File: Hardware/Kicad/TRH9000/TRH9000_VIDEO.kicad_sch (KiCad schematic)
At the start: 33 parts, among them J1 RGB, J2 S-Video, Q1 BC817, U6 CXA2075M

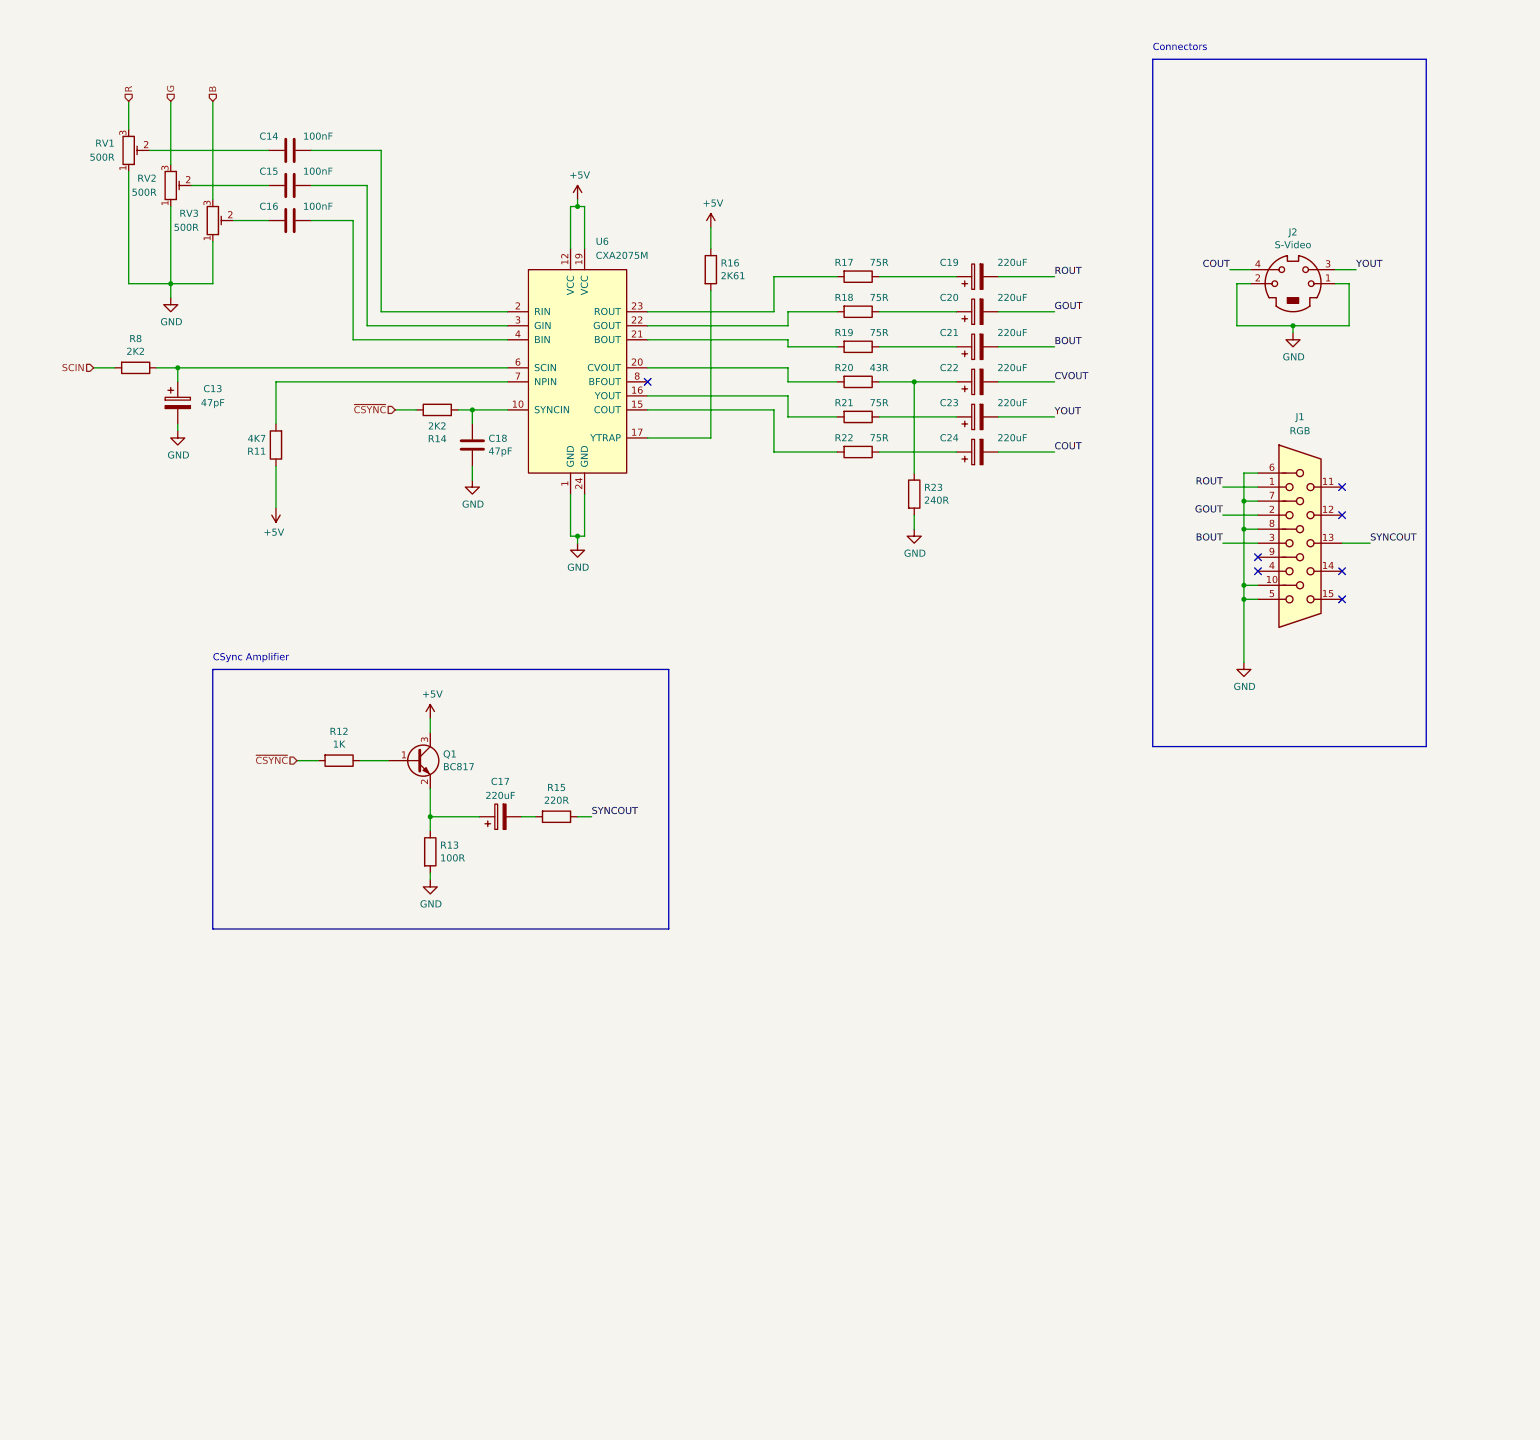
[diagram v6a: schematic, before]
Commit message: Many changes, among them, replacing the Composite out with SCART-rgb.
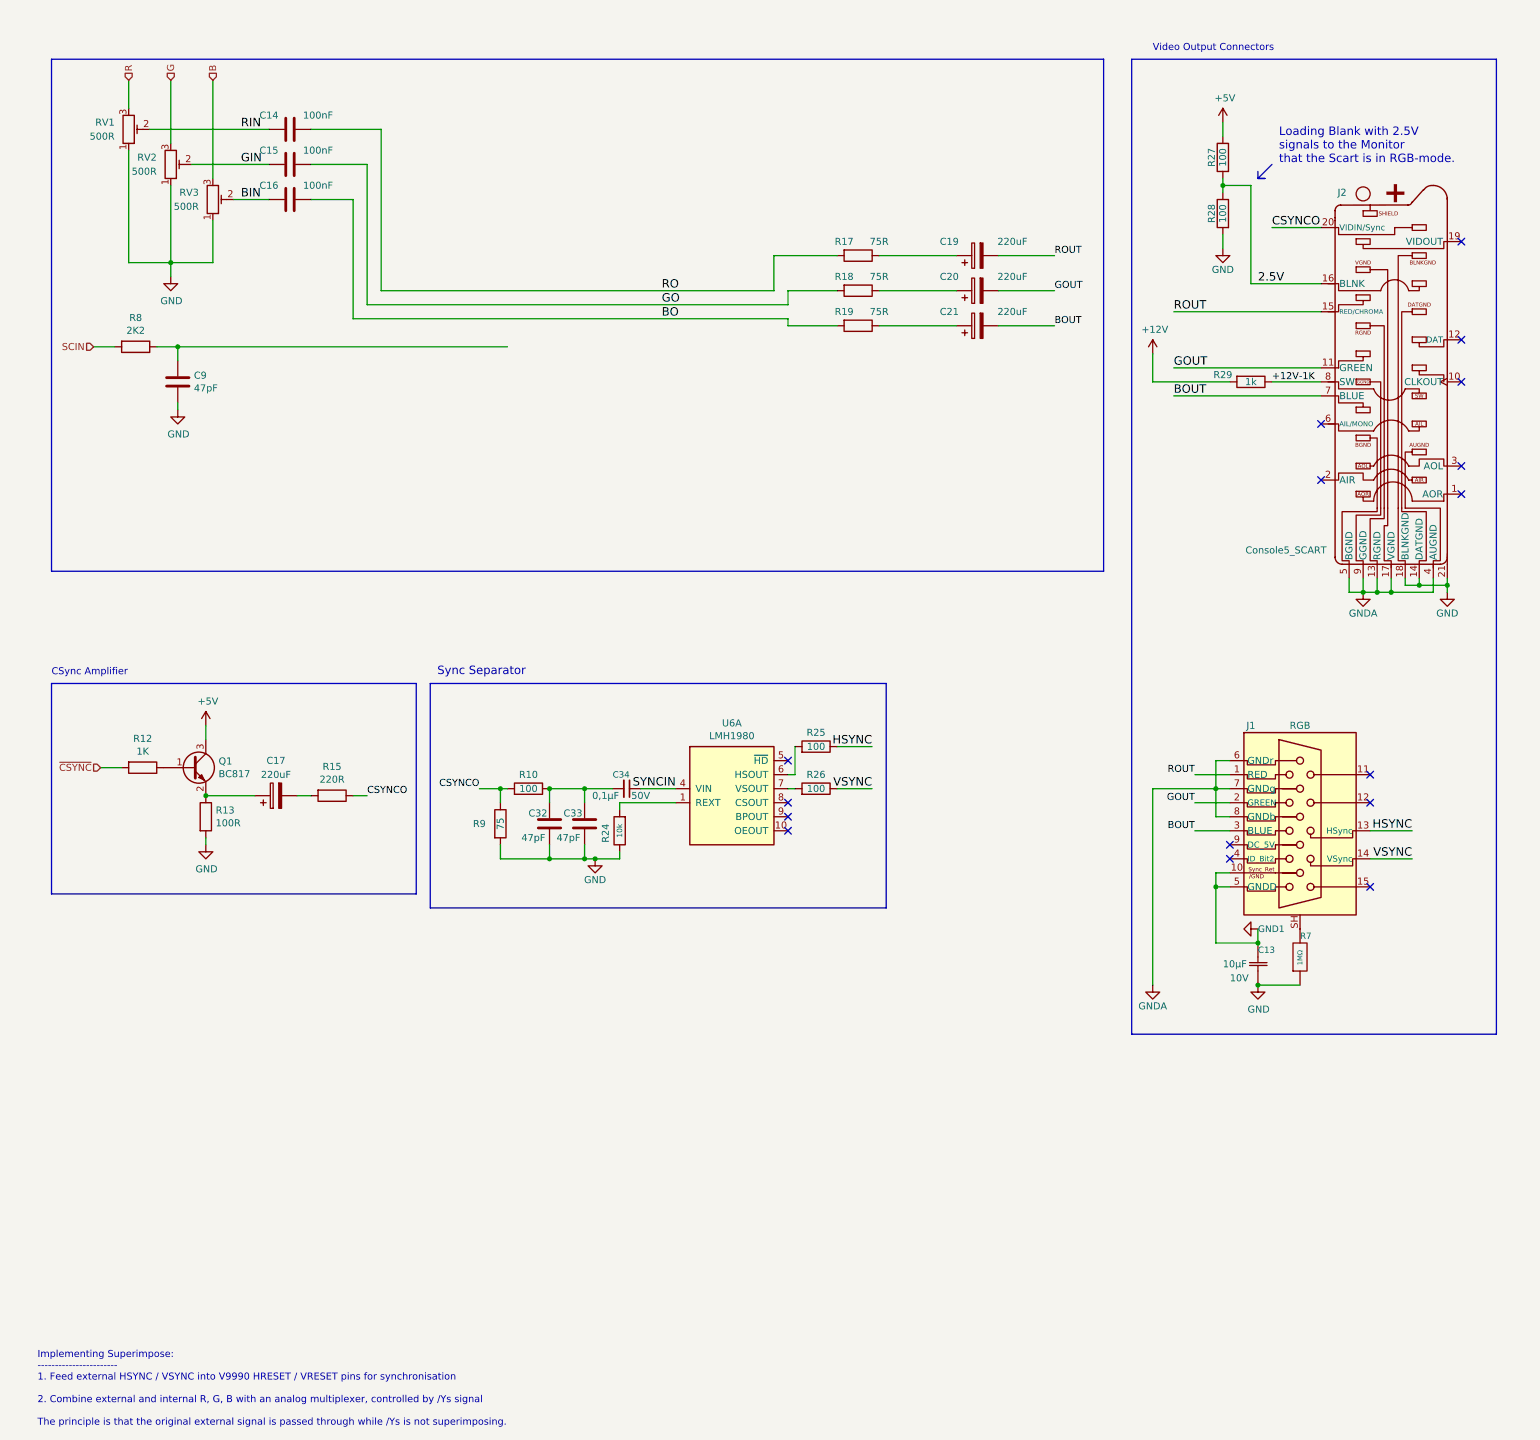
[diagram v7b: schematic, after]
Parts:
- removed C13: 47pF, Capacitor_THT:CP_Radial_D5.0mm_P2.50mm, symbol Device:C_Polarized
- removed C18: 47pF, Capacitor_SMD:C_0805_2012Metric, symbol Device:C
- removed C22, C23, C24: 220uF, Capacitor_THT:CP_Radial_D5.0mm_P2.50mm, symbol Device:C_Polarized
- removed J1: RGB, Connector_Dsub:DSUB-15-HD_Female_Horizontal_P2.29x1.98mm_EdgePinOffset3.03mm_Housed_MountingHolesOffset4.94mm, symbol Connector:DB15_Female_HighDensity
- removed J2: S-Video, Connector_PinHeader_2.54mm:PinHeader_1x04_P2.54mm_Vertical, symbol Connector:Mini-DIN-4
- removed R11: 4K7, Resistor_SMD:R_0805_2012Metric, symbol Device:R
- removed R14: 2K2, Resistor_SMD:R_0805_2012Metric, symbol Device:R
- removed R16: 2K61, Resistor_SMD:R_0805_2012Metric, symbol Device:R
- removed R20: 43R, Resistor_SMD:R_0805_2012Metric, symbol Device:R
- removed R21, R22: 75R, Resistor_SMD:R_0805_2012Metric, symbol Device:R
- removed R23: 240R, Resistor_SMD:R_0805_2012Metric, symbol Device:R
- removed U6: CXA2075M, Package_SO:SOP-24_7.5x15.4mm_P1.27mm, symbol TRH9000:CXA2075M
- added C13: C_GRM188D71A106KA73D, Capacitor_SMD:C_0603_1608Metric, symbol LRJ-parts:C_GRM188D71A106KA73D
- added C32, C33: 47pF, Capacitor_SMD:C_0603_1608Metric, symbol Device:C
- added C34: C_CL10B104KB8NNNL, Capacitor_SMD:C_0603_1608Metric_Pad1.08x0.95mm_HandSolder, symbol LRJ-parts:C_CL10B104KB8NNNL
- added C9: 47pF, Capacitor_SMD:C_0805_2012Metric, symbol Device:C
- added J1: RGB, LRJ:DSUB-Amphenol_L77HDE15SD1CH4RHNVGA, symbol LRJ-parts:Amphenol_L77HDE15SD1CH4RHNVGA
- added J2: Console5_SCART, LRJ:SCART-21_Female_Horizontal_P1.905x2.54mm_EdgePinOffset10.7mm, symbol LRJ-parts:Console5_SCART
- added R10, R25, R26, R27, R28: 100, Resistor_SMD:R_0603_1608Metric, symbol Device:R
- added R24: R_RC0603FR-0710KL, LRJ:R_0603_1608Metric_roundcourt, symbol LRJ-parts:R_RC0603FR-0710KL
- added R29: 1k, Resistor_SMD:R_0603_1608Metric, symbol Device:R
- added R7: R_ERJ-3GEYJ105V, Resistor_SMD:R_0603_1608Metric, symbol LRJ-parts:R_ERJ-3GEYJ105V
- added R9: 75, Resistor_SMD:R_0603_1608Metric, symbol Device:R
- added U6: LMH1980, Package_SO:VSSOP-10_3x3mm_P0.5mm, symbol LRJ-parts:LMH1980
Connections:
- net +5V: now also R27.1
- net BOUT: now also J1.3 (BLUE), J2.7 (BLUE)
- net GND: now also C13.1, C32.2, C33.2, C9.2, J2.14 (DATGND), J2.18 (BLNKGND), J2.21 (SH), R24.1, R28.2, R7.1, R9.2
- net GOUT: now also J1.2 (GREEN), J2.11 (GREEN)
- net ROUT: now also J1.1 (RED), J2.15 (RED/CHROMA)
- net GIN: now reaches C15.2, RV2.2
- net RO: now reaches C14.1
- net RO: now also R17.2
- net RIN: now reaches C14.2, RV1.2
- net at R8.1: now also C9.1
- net BIN: now reaches C16.2, RV3.2
- net BO: now reaches R19.2
- net BO: now also C16.1
- net GO: now reaches R18.2
- net GO: now also C15.1
- net SYNCOUT renamed CSYNCO
- net CSYNCO: now also J2.20 (VIDIN/Sync), R10.2, R9.1
- new net: J1.SH, R7.2
- new net: R26.2, U6.7 (VSOUT)
- new net: C32.1, C33.1, C34.2, R10.1
- new net: R25.2, U6.6 (HSOUT)
- new net: R24.2, U6.1 (REXT)
- new net +12V: R29.2
- new net +12V-1K: J2.8 (SW), R29.1
- new net 2.5V: J2.16 (BLNK), R27.2, R28.1
- new net GND1: C13.2, J1.10 (Sync_Ret/GND), J1.5 (GNDD)
- new net GNDA: J1.6 (GNDr), J1.7 (GNDg), J1.8 (GNDb), J2.13 (RGND), J2.17 (VGND), J2.4 (AUGND), J2.5 (BGND), J2.9 (GGND)
- new net HSYNC: J1.13 (HSync), R25.1
- new net SYNCIN: C34.1, U6.4 (VIN)
- new net VSYNC: J1.14 (VSync), R26.1
- no-connect marks 7 -> 16
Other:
- note added: "Implementing Superimpose: ----------------------- 1. Feed external HSYNC / VSYNC into V9990 HRESET / VRESET pins for synchronisation 2. Combine external and internal R, G, B with an analog multiplexer, controlled by /Ys signal The principle is that the original external signal is passed through while /Ys is not superimposing."
- note added: "Loading Blank with 2.5V signals to the Monitor that the Scart is in RGB-mode."
- note added: "Sync Separator"
- note added: "Video Output Connectors"
- note removed: "Connectors"
- moved on the sheet: C14, C15, C16, C17, C19, C20, C21, Q1, R12, R13, R15, R17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

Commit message: Multiple updates. Routing. Almost finished routing for the VDP. Moved back the footprint for the 14mhz oscillator to THT as it is easier to find outside US/Europe and I have a bunch laying around here. Organized all components into the PCB. Removed the holed in the cartridge so I can better measure them in the standard MSX cartridge. Changed the RGB connector footprint to a shorter version so we can fit it in the standard size cartridge. Fixed multiple footprints to 0805 as we will be standardizing in that size.
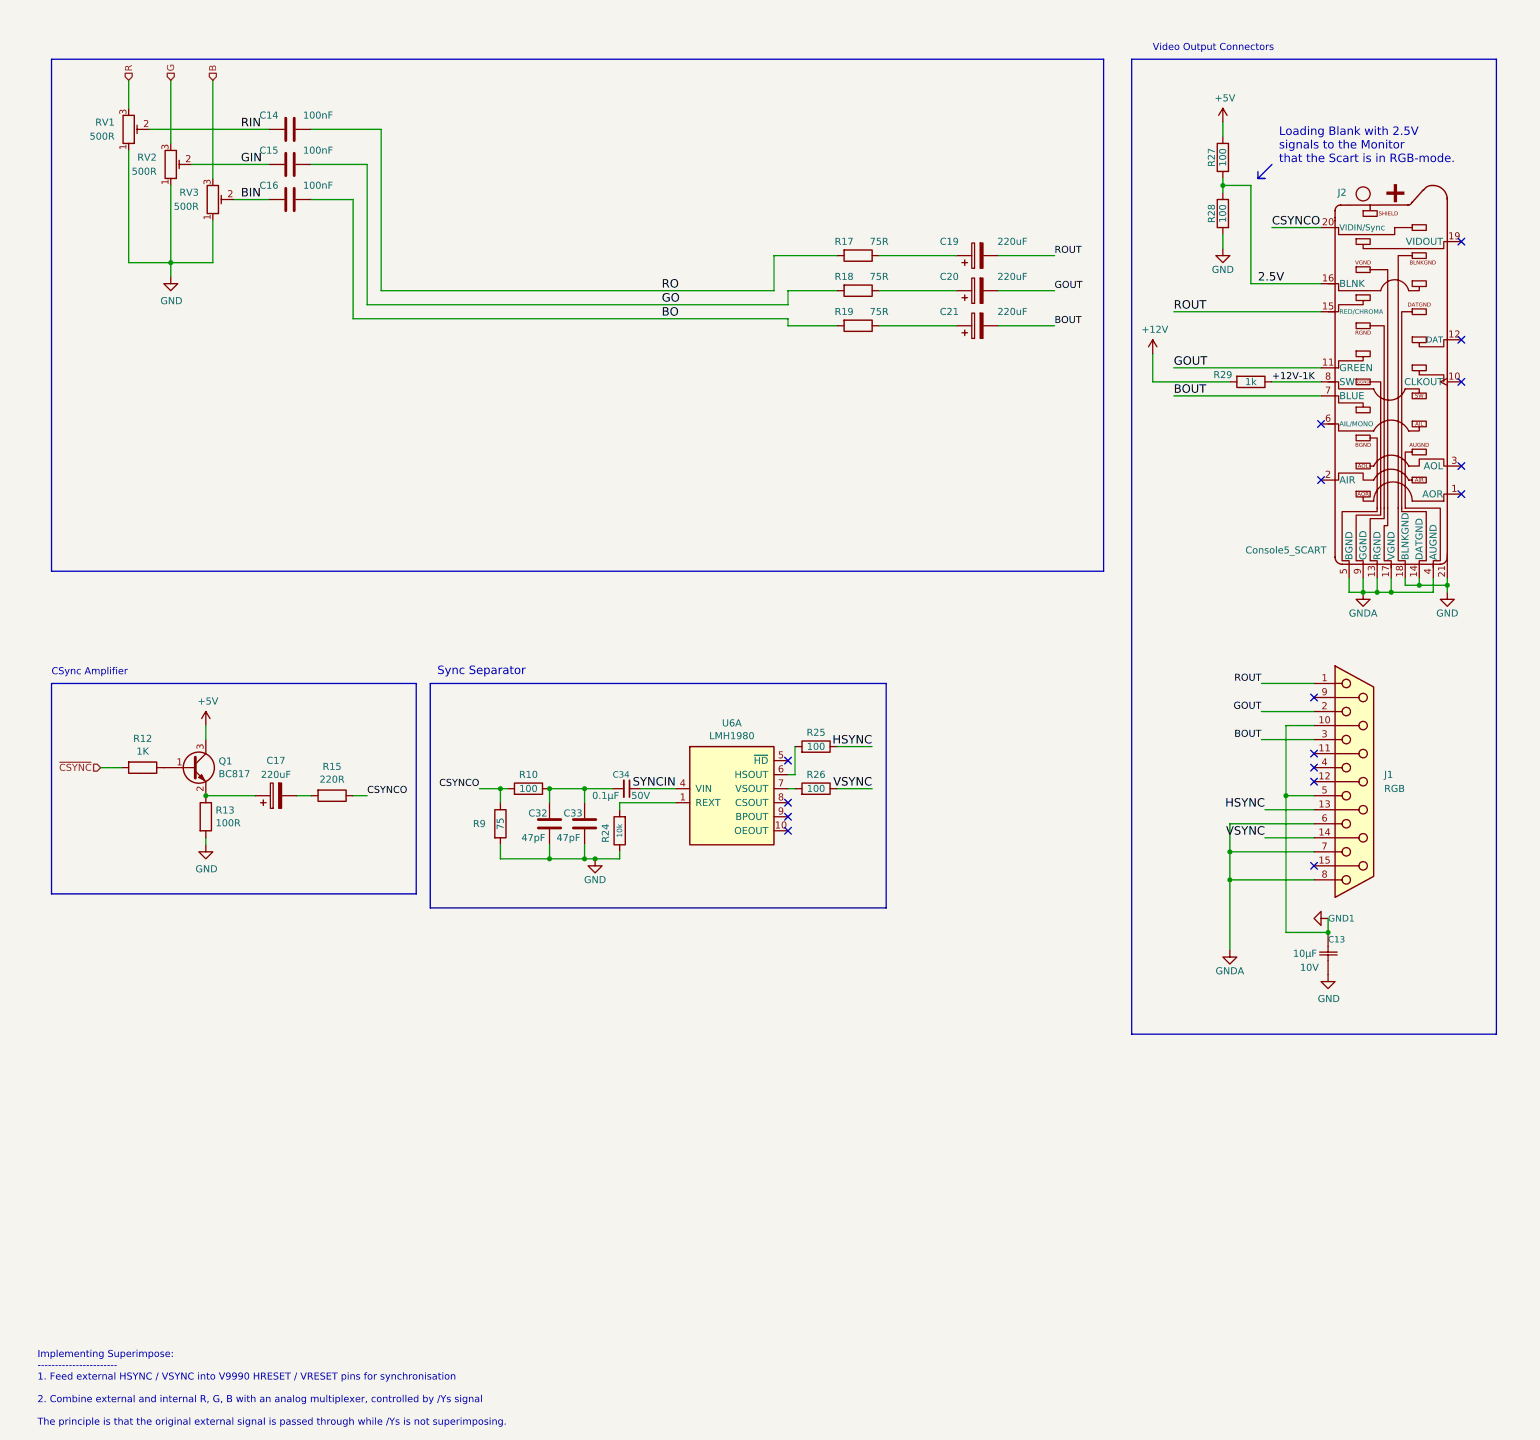
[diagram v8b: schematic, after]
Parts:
- removed C9: 47pF, Capacitor_SMD:C_0805_2012Metric, symbol Device:C
- removed J1: RGB, LRJ:DSUB-Amphenol_L77HDE15SD1CH4RHNVGA, symbol LRJ-parts:Amphenol_L77HDE15SD1CH4RHNVGA
- removed R7: R_ERJ-3GEYJ105V, Resistor_SMD:R_0603_1608Metric, symbol LRJ-parts:R_ERJ-3GEYJ105V
- removed R8: 2K2, Resistor_SMD:R_0805_2012Metric, symbol Device:R
- added J1: RGB, Connector_Dsub:DSUB-15-HD_Female_Horizontal_P2.29x1.98mm_EdgePinOffset3.03mm_Housed_MountingHolesOffset4.94mm, symbol Connector:DB15_Female
- C13: value C_GRM188D71A106KA73D -> 10µF; footprint Capacitor_SMD:C_0603_1608Metric -> Capacitor_SMD:C_0805_2012Metric
- C32, C33: footprint Capacitor_SMD:C_0603_1608Metric -> Capacitor_SMD:C_0805_2012Metric
- C34: value C_CL10B104KB8NNNL -> 0.1µF; footprint Capacitor_SMD:C_0603_1608Metric_Pad1.08x0.95mm_HandSolder -> Capacitor_SMD:C_0805_2012Metric; Capacitance  0,1µF -> 0.1µF
- R10, R25, R26, R9: footprint Resistor_SMD:R_0603_1608Metric -> Resistor_SMD:R_0805_2012Metric
- R24: value R_RC0603FR-0710KL -> 10k; footprint LRJ:R_0603_1608Metric_roundcourt -> Capacitor_SMD:C_0805_2012Metric
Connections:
- net BOUT: now also J1.3
- net GND1: now also J1.10 (P10), J1.5
- net GNDA: now also J1.6, J1.7, J1.8
- net GOUT: now also J1.2
- net HSYNC: now also J1.13 (P13)
- net ROUT: now also J1.1
- net VSYNC: now also J1.14 (P14)
